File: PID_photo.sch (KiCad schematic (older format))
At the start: 31 parts

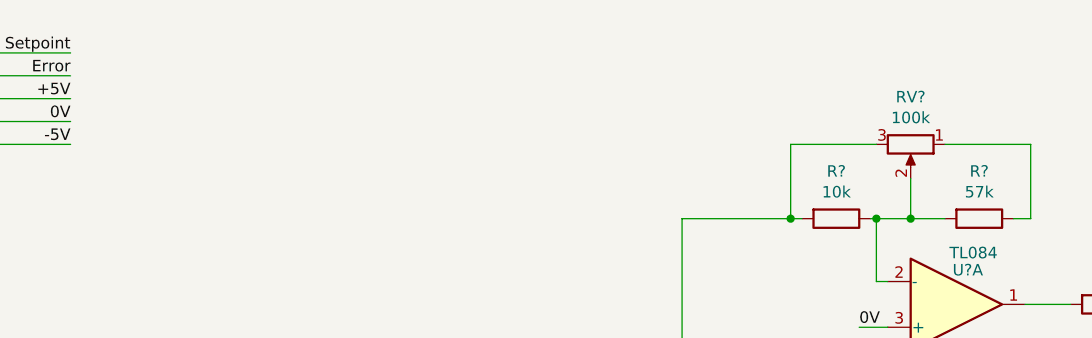
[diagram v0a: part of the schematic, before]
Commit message: Added PIDs blocks
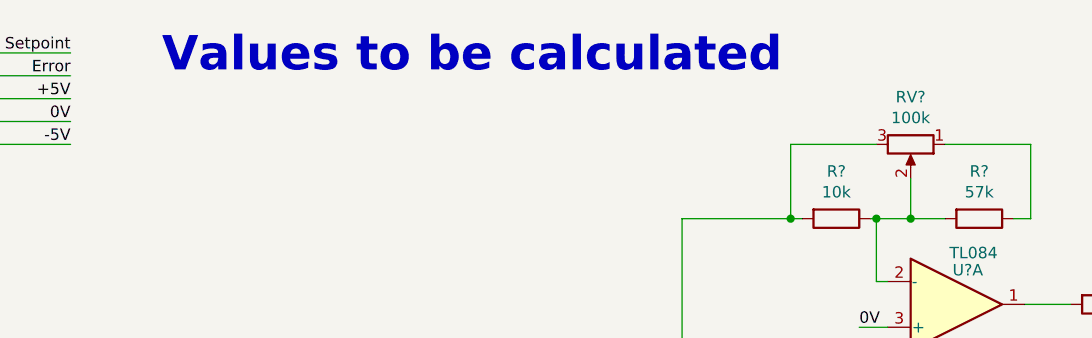
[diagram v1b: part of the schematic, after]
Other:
- note added: "Values to be calculated"
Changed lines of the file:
@@
 $Descr A4 11693 8268
 encoding utf-8
-Sheet 9 12
+Sheet 11 12
 Title ""
 Date ""
@@
 U 1 1 6190CEB3
 P 5150 1700
+AR Path="/619B51F3/6190CEB3" Ref="U?"  Part="1"
+AR Path="/61820F6B/6190CEB3" Ref="U?"  Part="1"
+AR Path="/61A28785/6190CEB3" Ref="U?"  Part="1"
 F 0 "U?" H 5200 1550 50  0000 C CNN
 F 1 "TL084" H 5225 1475 50  0000 C CNN
@@
 U 2 1 6190EA94
 P 5150 2900
+AR Path="/619B51F3/6190EA94" Ref="U?"  Part="2"
+AR Path="/61820F6B/6190EA94" Ref="U?"  Part="2"
+AR Path="/61A28785/6190EA94" Ref="U?"  Part="2"
 F 0 "U?" H 5150 2725 50  0000 C CNN
 F 1 "TL084" H 5175 2650 50  0000 C CNN
@@
 U 3 1 61910199
 P 5150 3975
+AR Path="/619B51F3/61910199" Ref="U?"  Part="3"
+AR Path="/61820F6B/61910199" Ref="U?"  Part="3"
+AR Path="/61A28785/61910199" Ref="U?"  Part="3"
 F 0 "U?" H 5150 3800 50  0000 C CNN
 F 1 "TL084" H 5175 3725 50  0000 C CNN
@@
 U 4 1 619111F1
 P 6900 3000
+AR Path="/619B51F3/619111F1" Ref="U?"  Part="4"
+AR Path="/61820F6B/619111F1" Ref="U?"  Part="4"
+AR Path="/61A28785/619111F1" Ref="U?"  Part="4"
 F 0 "U?" H 6900 2825 50  0000 C CNN
 F 1 "TL084" H 6925 2750 50  0000 C CNN
@@
 U 5 1 619124C1
 P 1850 6950
+AR Path="/619B51F3/619124C1" Ref="U?"  Part="5"
+AR Path="/61820F6B/619124C1" Ref="U?"  Part="5"
+AR Path="/61A28785/619124C1" Ref="U?"  Part="5"
 F 0 "U?" H 1808 6996 50  0000 L CNN
 F 1 "TL084" H 1808 6905 50  0000 L CNN
@@
 U 1 1 619347E4
 P 1350 6750
+AR Path="/619B51F3/619347E4" Ref="C?"  Part="1"
+AR Path="/61820F6B/619347E4" Ref="C?"  Part="1"
+AR Path="/61A28785/619347E4" Ref="C?"  Part="1"
 F 0 "C?" H 1465 6796 50  0000 L CNN
 F 1 "100n" H 1465 6705 50  0000 L CNN
@@
 U 1 1 6193524E
 P 1350 7150
+AR Path="/619B51F3/6193524E" Ref="C?"  Part="1"
+AR Path="/61820F6B/6193524E" Ref="C?"  Part="1"
+AR Path="/61A28785/6193524E" Ref="C?"  Part="1"
 F 0 "C?" H 1465 7196 50  0000 L CNN
 F 1 "100n" H 1465 7105 50  0000 L CNN
@@
 U 1 1 61935E4A
 P 4625 1325
+AR Path="/619B51F3/61935E4A" Ref="R?"  Part="1"
+AR Path="/61820F6B/61935E4A" Ref="R?"  Part="1"
+AR Path="/61A28785/61935E4A" Ref="R?"  Part="1"
 F 0 "R?" V 4418 1325 50  0000 C CNN
 F 1 "10k" V 4509 1325 50  0000 C CNN
@@
 U 1 1 619366A7
 P 5250 1325
+AR Path="/619B51F3/619366A7" Ref="R?"  Part="1"
+AR Path="/61820F6B/619366A7" Ref="R?"  Part="1"
+AR Path="/61A28785/619366A7" Ref="R?"  Part="1"
 F 0 "R?" V 5043 1325 50  0000 C CNN
 F 1 "57k" V 5134 1325 50  0000 C CNN
@@
 U 1 1 619368E6
 P 5800 1700
+AR Path="/619B51F3/619368E6" Ref="R?"  Part="1"
+AR Path="/61820F6B/619368E6" Ref="R?"  Part="1"
+AR Path="/61A28785/619368E6" Ref="R?"  Part="1"
 F 0 "R?" V 5593 1700 50  0000 C CNN
 F 1 "10k" V 5684 1700 50  0000 C CNN
@@
 U 1 1 61936FF4
 P 4950 1000
+AR Path="/619B51F3/61936FF4" Ref="RV?"  Part="1"
+AR Path="/61820F6B/61936FF4" Ref="RV?"  Part="1"
+AR Path="/61A28785/61936FF4" Ref="RV?"  Part="1"
 F 0 "RV?" V 4743 1000 50  0000 C CNN
 F 1 "100k" V 4834 1000 50  0000 C CNN
@@
 U 1 1 61943F9E
 P 4825 2200
+AR Path="/619B51F3/61943F9E" Ref="RV?"  Part="1"
+AR Path="/61820F6B/61943F9E" Ref="RV?"  Part="1"
+AR Path="/61A28785/61943F9E" Ref="RV?"  Part="1"
 F 0 "RV?" V 4618 2200 50  0000 C CNN
 F 1 "1M" V 4709 2200 50  0000 C CNN
@@
 U 1 1 61944E14
 P 5075 2500
+AR Path="/619B51F3/61944E14" Ref="R?"  Part="1"
+AR Path="/61820F6B/61944E14" Ref="R?"  Part="1"
+AR Path="/61A28785/61944E14" Ref="R?"  Part="1"
 F 0 "R?" V 4868 2500 50  0000 C CNN
 F 1 "470k" V 4959 2500 50  0000 C CNN
@@
 U 1 1 6194AB1B
 P 5800 2900
+AR Path="/619B51F3/6194AB1B" Ref="R?"  Part="1"
+AR Path="/61820F6B/6194AB1B" Ref="R?"  Part="1"
+AR Path="/61A28785/6194AB1B" Ref="R?"  Part="1"
 F 0 "R?" V 5593 2900 50  0000 C CNN
 F 1 "10k" V 5684 2900 50  0000 C CNN
@@
 U 1 1 6194CA5C
 P 4575 2800
+AR Path="/619B51F3/6194CA5C" Ref="R?"  Part="1"
+AR Path="/61820F6B/6194CA5C" Ref="R?"  Part="1"
+AR Path="/61A28785/6194CA5C" Ref="R?"  Part="1"
 F 0 "R?" V 4368 2800 50  0000 C CNN
 F 1 "10k" V 4459 2800 50  0000 C CNN
@@
 U 1 1 6194E347
 P 4200 2800
+AR Path="/619B51F3/6194E347" Ref="C?"  Part="1"
+AR Path="/61820F6B/6194E347" Ref="C?"  Part="1"
+AR Path="/61A28785/6194E347" Ref="C?"  Part="1"
 F 0 "C?" V 3948 2800 50  0000 C CNN
 F 1 "220n" V 4039 2800 50  0000 C CNN
@@
 U 1 1 61951D7A
 P 4575 3575
+AR Path="/619B51F3/61951D7A" Ref="RV?"  Part="1"
+AR Path="/61820F6B/61951D7A" Ref="RV?"  Part="1"
+AR Path="/61A28785/61951D7A" Ref="RV?"  Part="1"
 F 0 "RV?" V 4368 3575 50  0000 C CNN
 F 1 "100k" V 4459 3575 50  0000 C CNN
@@
 U 1 1 61956CC5
 P 4375 3875
+AR Path="/619B51F3/61956CC5" Ref="R?"  Part="1"
+AR Path="/61820F6B/61956CC5" Ref="R?"  Part="1"
+AR Path="/61A28785/61956CC5" Ref="R?"  Part="1"
 F 0 "R?" V 4168 3875 50  0000 C CNN
 F 1 "22k" V 4259 3875 50  0000 C CNN
@@
 U 1 1 6195B27F
 P 5125 3575
+AR Path="/619B51F3/6195B27F" Ref="C?"  Part="1"
+AR Path="/61820F6B/6195B27F" Ref="C?"  Part="1"
+AR Path="/61A28785/6195B27F" Ref="C?"  Part="1"
 F 0 "C?" V 4873 3575 50  0000 C CNN
 F 1 "100n" V 4964 3575 50  0000 C CNN
@@
 U 1 1 619625D8
 P 5800 3975
+AR Path="/619B51F3/619625D8" Ref="R?"  Part="1"
+AR Path="/61820F6B/619625D8" Ref="R?"  Part="1"
+AR Path="/61A28785/619625D8" Ref="R?"  Part="1"
 F 0 "R?" V 5593 3975 50  0000 C CNN
 F 1 "10k" V 5684 3975 50  0000 C CNN
@@
 U 1 1 61982F00
 P 6875 2625
+AR Path="/619B51F3/61982F00" Ref="R?"  Part="1"
+AR Path="/61820F6B/61982F00" Ref="R?"  Part="1"
+AR Path="/61A28785/61982F00" Ref="R?"  Part="1"
 F 0 "R?" V 6668 2625 50  0000 C CNN
 F 1 "10k" V 6759 2625 50  0000 C CNN
@@
 U 1 1 619938D0
 P 7425 3000
+AR Path="/619B51F3/619938D0" Ref="R?"  Part="1"
+AR Path="/61820F6B/619938D0" Ref="R?"  Part="1"
+AR Path="/61A28785/619938D0" Ref="R?"  Part="1"
 F 0 "R?" V 7218 3000 50  0000 C CNN
 F 1 "1k" V 7309 3000 50  0000 C CNN
@@
 U 1 1 619A4A1D
 P 3250 2300
+AR Path="/619B51F3/619A4A1D" Ref="R?"  Part="1"
+AR Path="/61820F6B/619A4A1D" Ref="R?"  Part="1"
+AR Path="/61A28785/619A4A1D" Ref="R?"  Part="1"
 F 0 "R?" V 3043 2300 50  0000 C CNN
 F 1 "10k" V 3134 2300 50  0000 C CNN
@@
 U 1 1 6199C115
 P 3250 2800
+AR Path="/619B51F3/6199C115" Ref="U?"  Part="1"
+AR Path="/61820F6B/6199C115" Ref="U?"  Part="1"
+AR Path="/61A28785/6199C115" Ref="U?"  Part="1"
 F 0 "U?" H 3300 2925 50  0000 L CNN
 F 1 "TL071" H 3300 3000 50  0000 L CNN
@@
 U 1 1 619AE2CE
 P 2475 6950
+AR Path="/619B51F3/619AE2CE" Ref="C?"  Part="1"
+AR Path="/61820F6B/619AE2CE" Ref="C?"  Part="1"
+AR Path="/61A28785/619AE2CE" Ref="C?"  Part="1"
 F 0 "C?" H 2590 6996 50  0000 L CNN
 F 1 "100n" H 2590 6905 50  0000 L CNN
@@
 U 1 1 619D83AD
 P 2650 2900
+AR Path="/619B51F3/619D83AD" Ref="R?"  Part="1"
+AR Path="/61820F6B/619D83AD" Ref="R?"  Part="1"
+AR Path="/61A28785/619D83AD" Ref="R?"  Part="1"
 F 0 "R?" V 2750 2900 50  0000 C CNN
 F 1 "10k" V 2825 2900 50  0000 C CNN
@@
 U 1 1 619D9316
 P 2875 3125
+AR Path="/619B51F3/619D9316" Ref="R?"  Part="1"
+AR Path="/61820F6B/619D9316" Ref="R?"  Part="1"
+AR Path="/61A28785/619D9316" Ref="R?"  Part="1"
 F 0 "R?" H 2805 3079 50  0000 R CNN
 F 1 "10k" H 2805 3170 50  0000 R CNN
@@
 U 1 1 619E4FE6
 P 2650 2700
+AR Path="/619B51F3/619E4FE6" Ref="R?"  Part="1"
+AR Path="/61820F6B/619E4FE6" Ref="R?"  Part="1"
+AR Path="/61A28785/619E4FE6" Ref="R?"  Part="1"
 F 0 "R?" V 2857 2700 50  0000 C CNN
 F 1 "10k" V 2766 2700 50  0000 C CNN
@@
 U 1 1 61A012A2
 P 2250 3125
+AR Path="/619B51F3/61A012A2" Ref="C?"  Part="1"
+AR Path="/61820F6B/61A012A2" Ref="C?"  Part="1"
+AR Path="/61A28785/61A012A2" Ref="C?"  Part="1"
 F 0 "C?" H 2135 3079 50  0000 R CNN
 F 1 "10u" H 2135 3170 50  0000 R CNN
@@
 U 1 1 61A023B8
 P 1900 3125
+AR Path="/619B51F3/61A023B8" Ref="C?"  Part="1"
+AR Path="/61820F6B/61A023B8" Ref="C?"  Part="1"
+AR Path="/61A28785/61A023B8" Ref="C?"  Part="1"
 F 0 "C?" H 1785 3079 50  0000 R CNN
 F 1 "10u" H 1785 3170 50  0000 R CNN
@@
 U 1 1 61A1C984
 P 1675 2900
+AR Path="/619B51F3/61A1C984" Ref="R?"  Part="1"
+AR Path="/61820F6B/61A1C984" Ref="R?"  Part="1"
+AR Path="/61A28785/61A1C984" Ref="R?"  Part="1"
 F 0 "R?" V 1882 2900 50  0000 C CNN
 F 1 "4k7" V 1791 2900 50  0000 C CNN
@@
 Wire Wire Line
 	1200 2900 1525 2900
+Text Notes 1675 700  0    150  ~ 30
+Values to be calculated
 $EndSCHEMATC

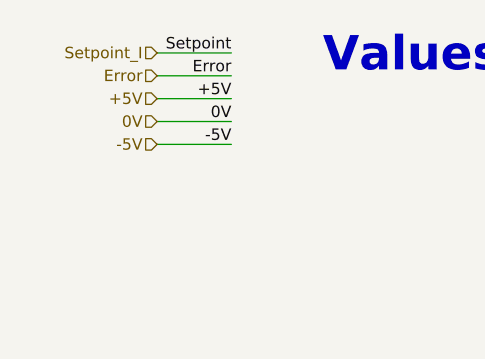
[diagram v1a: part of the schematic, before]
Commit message: Added jumpers to PID blocks
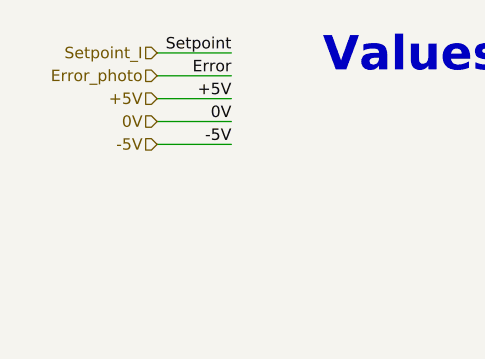
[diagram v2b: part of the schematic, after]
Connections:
- net Error renamed Error_photo
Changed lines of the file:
@@
 Setpoint_I
 Text HLabel 950  700  0    50   Input ~ 0
-Error
+Error_photo
 Text HLabel 950  800  0    50   Input ~ 0
 +5V
